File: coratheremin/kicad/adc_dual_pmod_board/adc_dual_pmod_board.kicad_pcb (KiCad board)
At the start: 2 copper layers, 45.7 x 57.2 mm, 63 parts, among them J1 PITCH, J2 VOLUME, J3 PMOD_A, J4 PMOD_B, J5 AUX1, U1 LP2985-4.5, U2 LP2985-4.5, U3 LP2985-3.3, U4 LP2985-3.3, U5 AD9283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

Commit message: update PCBs
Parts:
- U5, U6: footprint Package_SO:SSOP-20_4.4x6.5mm_P0.65mm -> Package_SO:SSOP-20_5.3x7.2mm_P0.65mm
- moved C1 2.54 mm to (88.9, 67.7)
- moved C11 2.54 mm to (78.1, 59.5)
- moved C12 2.54 mm to (78.1, 82.3)
- moved C13 2.54 mm to (70.9, 61.0)
- moved C14 2.54 mm to (70.9, 58.4)
- moved C15 2.54 mm to (70.9, 83.8)
- moved C16 2.54 mm to (70.9, 81.3)
- moved C19 2.54 mm to (72.8, 50.2)
- moved C2 2.54 mm to (83.2, 74.7)
- moved C29 2.54 mm to (69.2, 51.0)
- moved C3 2.54 mm to (83.2, 67.7)
- moved C4 2.54 mm to (88.9, 74.7)
- moved C5 2.54 mm to (88.9, 61.2)
- moved C6 2.54 mm to (88.9, 82.8)
- moved J1 2.54 mm to (86.4, 55.9)
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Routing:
- net +5V: track 91.2 -> 60.9 mm, vias 1 -> 0
- net /CLK: track 30.2 -> 0.00 mm
- net GND2: track 119.3 -> 99.0 mm, vias 13 -> 7
- net GND: track 113.5 -> 97.2 mm, vias 12 -> 6
- net +3V3: track 17.7 -> 12.0 mm
- net +3.3VA: track 17.7 -> 12.0 mm
- net Net-(C25-Pad1): track 3.32 -> 5.50 mm
- net Net-(C26-Pad1): track 3.32 -> 5.47 mm
- net /VaD_B: track 29.2 -> 31.0 mm
- net /AIN_N: track 7.18 -> 8.05 mm
- net /VaD_A: track 29.4 -> 30.1 mm
- net /BIN_N: track 7.14 -> 7.74 mm
- net /BIN_P: track 7.44 -> 8.03 mm
- net /AIN_P: track 7.44 -> 8.02 mm
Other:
- board size 45.7 x 57.2 mm -> 49.5 x 57.2 mm
- board text added: "2x100MHz 8bit ADC for CoraZ7 Theremin rev0.1"
- board text added: "3.3V"

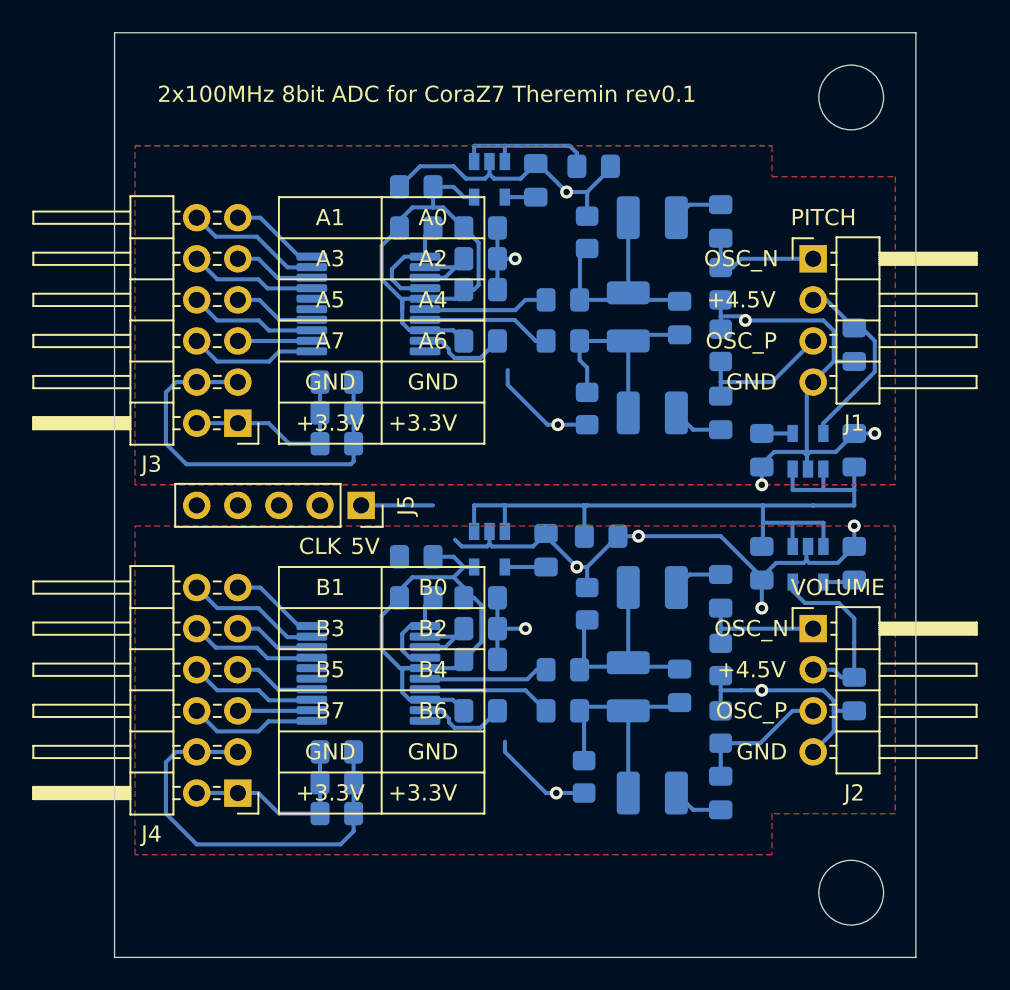
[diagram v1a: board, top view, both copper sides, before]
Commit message: cora z7 theremin dual 100MHz ADC pmods board
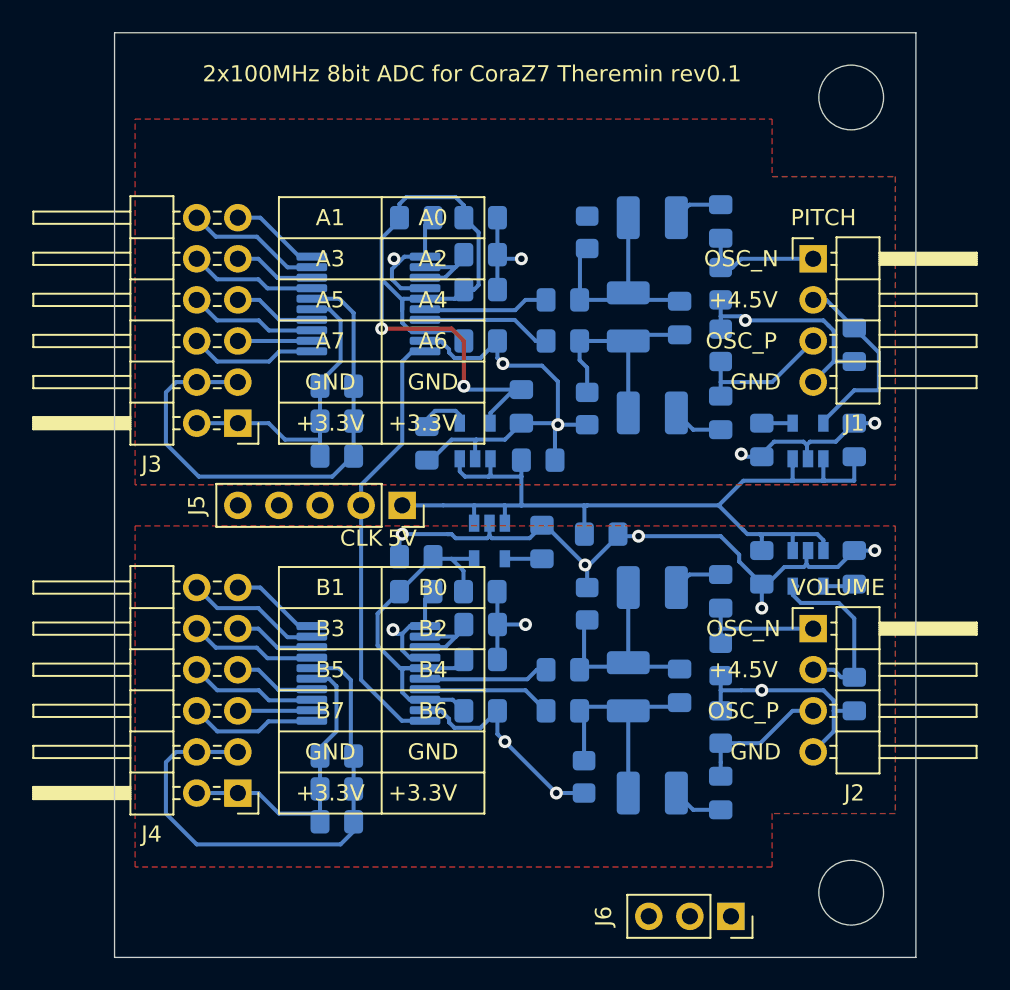
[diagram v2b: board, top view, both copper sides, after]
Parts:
- added J6: Conn_mount, Connector_PinSocket_2.54mm:PinSocket_1x03_P2.54mm_Vertical, F.Cu at (81.3, 96.5)
- moved C19 18.5 mm to (69.4, 68.3)
- moved C29 17.6 mm to (62.5, 67.3), turned to 270 degrees
- moved U3 16.2 mm to (65.5, 67.1), turned to 90 degrees
- moved C31 15.0 mm to (68.3, 65.0), turned to 270 degrees
- moved J5 2.54 mm to (61.0, 71.1)
- moved C33 0.76 mm to (56.9, 68.1)
- moved C1 0.64 mm to (88.9, 67.1)
- moved C3 0.64 mm to (83.2, 67.1)
- moved U1 0.64 mm to (86.0, 67.1)
- moved C17 0.63 mm to (61.8, 53.3)
- moved C21 0.63 mm to (65.8, 53.3)
- moved C30 0.57 mm to (69.6, 73.4)
- moved C34 0.51 mm to (56.9, 90.7)
- moved C37 0.51 mm to (56.9, 65.9)
- moved U4 0.51 mm to (66.4, 73.3)
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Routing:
- net /CLK: track 0.00 -> 27.4 mm
- net GND2: track 99.0 -> 115.4 mm, vias 7 -> 10
- net /VaD_A: track 30.1 -> 45.7 mm, vias 0 -> 2
- net +3V3: track 12.0 -> 19.1 mm
- net +3.3VA: track 12.0 -> 18.2 mm
- net /VaD_B: track 31.0 -> 25.1 mm
- net +5V: track 60.9 -> 56.1 mm
- net GND: track 97.2 -> 99.2 mm, vias 6 -> 7
- net Net-(C29-Pad1): track 1.91 -> 3.32 mm

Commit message: update ADC board pcb, replace ssop20 footprint
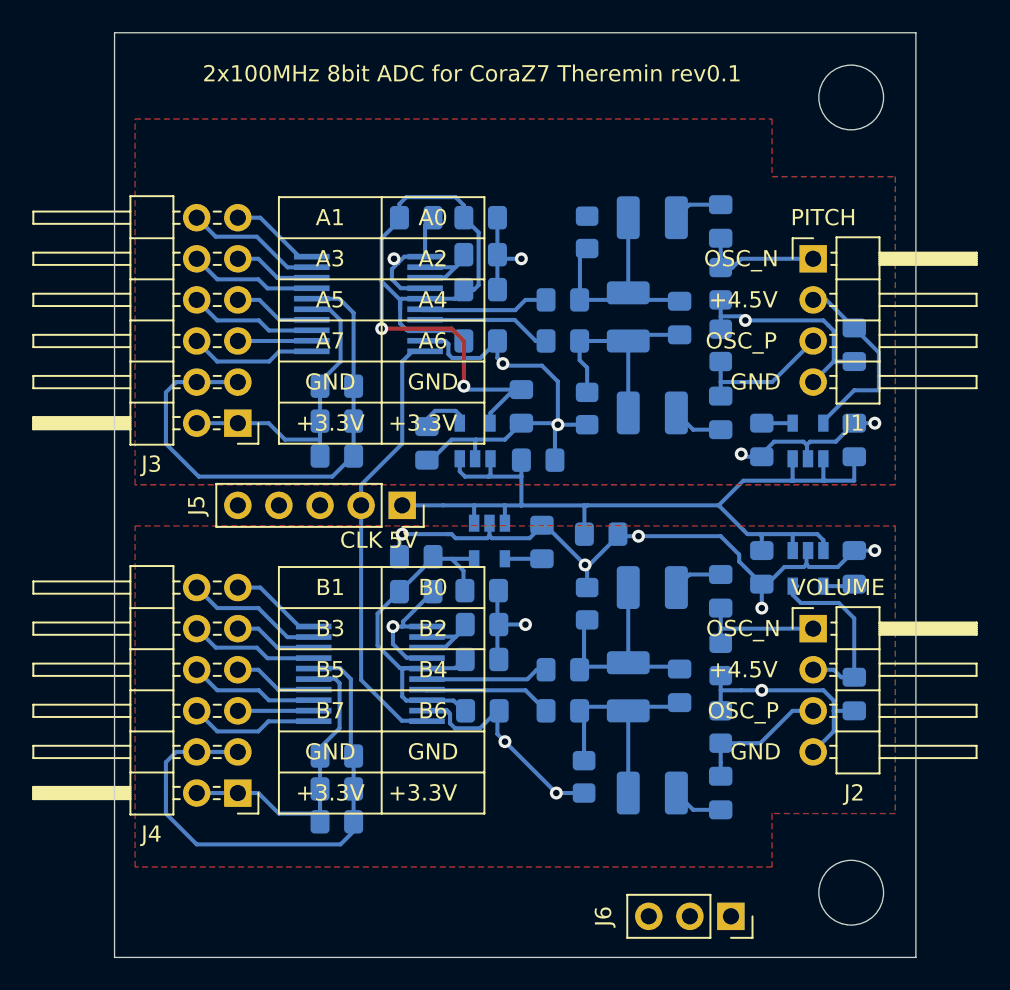
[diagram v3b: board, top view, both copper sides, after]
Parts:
- U5, U6: footprint Package_SO:SSOP-20_5.3x7.2mm_P0.65mm -> ssop-20_custom:SSOP-20-wide-7-P0.65
- moved U6 0.12 mm to (59.0, 81.5)
- moved C22 0.11 mm to (65.9, 76.4)
- moved C28 0.11 mm to (65.9, 83.8)
- moved C24 0.08 mm to (65.9, 80.6)
- moved C26 0.08 mm to (65.9, 78.5)
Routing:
- net GND2: track 115.4 -> 117.1 mm
